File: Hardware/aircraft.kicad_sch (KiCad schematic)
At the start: 0 parts

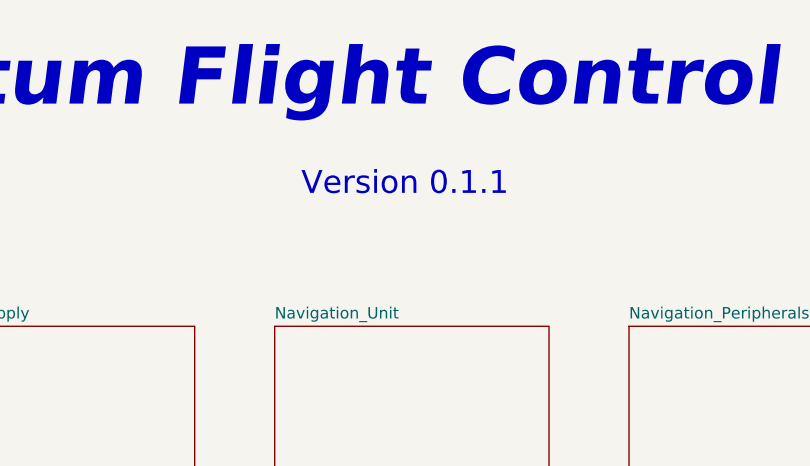
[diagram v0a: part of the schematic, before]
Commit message: hardware version 0.1.2, minor improvements and footprint selection (missing some gnss and bulk regulator components
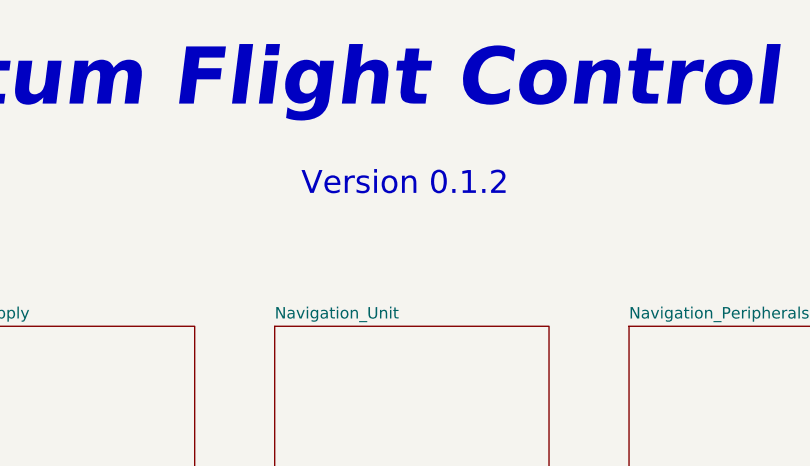
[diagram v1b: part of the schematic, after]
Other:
- note added: "Version 0.1.2"
- note removed: "Version 0.1.1"
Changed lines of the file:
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@@
 	(title_block
 		(title "Gravitum Flight Control System")
-		(rev "0.1.0")
+		(rev "0.1.2")
 		(company "Breno Soares Alves")
 	)
@@
 		)
 	)
-	(text "Version 0.1.1"
+	(text "Version 0.1.2"
 		(exclude_from_sim no)
 		(at 149.098 51.562 0)
